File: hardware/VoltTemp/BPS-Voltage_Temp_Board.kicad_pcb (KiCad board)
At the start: 4 copper layers, 98.4 x 81.3 mm, 149 parts, among them IC1 ISO1641BDR, J1 ScrutineeringConn, J10 53307-2471, J11 Conn_01x07, J3 Conn_01x05, J4 Conn_01x05, J5 Logic_Analyzer, J8 Conn_01x06, J9 Conn_01x03, T1 TP_TempOut, T2 TP_TempOut, T3 TP_TempOut, T4 TP_TempOut, T5 TP_TempOut, U1 EL3H7, U12 TLV9062xD, U13 TLV9062xD, U14 TLV9062xD, U2 BQ7692003PW, U3 EL3H7, U4 TLV9062xD, U6 TLV9062xD

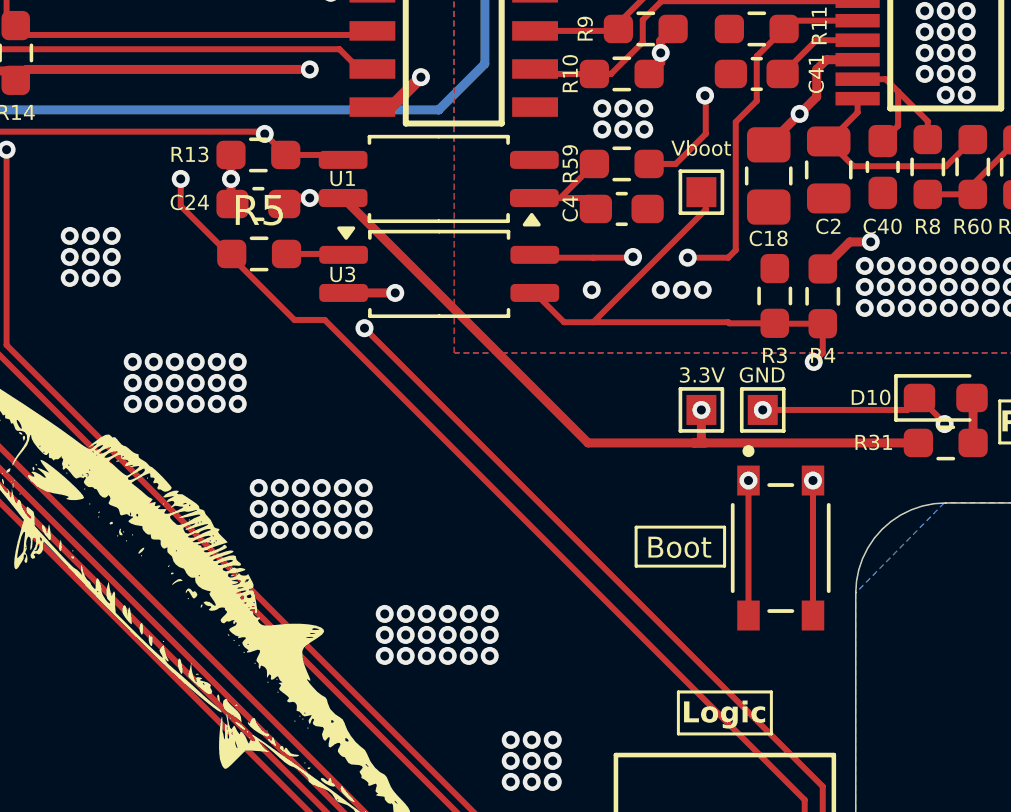
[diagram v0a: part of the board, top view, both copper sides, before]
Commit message: fixed switch label, some silkscreen
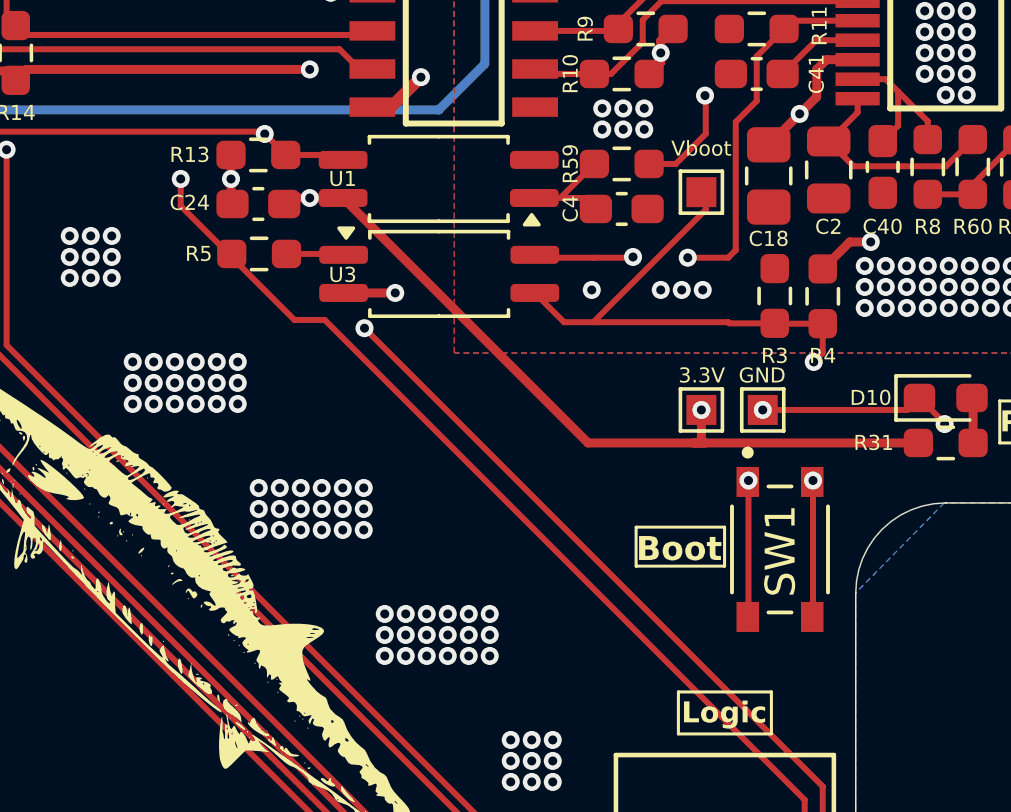
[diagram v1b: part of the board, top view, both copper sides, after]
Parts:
- removed Boot: BOOT, VoltTemp:SW_TL3365AF180QG
- added SW1: BOOT, VoltTemp:SW_TL3365AF180QG, F.Cu at (66.3, 71.5)
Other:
- board text added: "Boot"
